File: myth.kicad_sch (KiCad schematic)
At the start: 151 parts, among them J1 Conn_01x08_Male, J2 Conn_01x08_Male, J4 Conn_01x08_Male, J5 Conn_01x08_Male, J6 Conn_01x08_Male, U1 74AHC02, U10 74HC595, U100 74AHC08, U101 74LS32, U102 74LS08, U103 74HC00, U104 74LS08, U105 74AHC02, U106 74LS08, U107 74LS08, U108 74LS08, U109 74LS573, U11 74HC165, U110 74LS573, U111 74HC157, U112 74HC157, U113 74HC157, U114 74AHC08, U115 4002, U116 4072, U117 74LS573, U118 74LS32, U119 74LS573, U12 74AHC08, U120 74LS573, U121 74AHC273, U122 74HC157, U123 74LS32, U124 74AHC04, U125 74LS573, U126 74LS573, U127 74AHC08, U128 74LS27, U129 74HC00, U13 74HC238, U130 74AHC08, U131 74LS573, U132 74HC74, U133 4072, U134 4072, U135 4078, U136 74AHC244, U137 74LS32, U138 74LS32, U139 74AHC273, U14 74HC238, U140 74LS32, U141 74LS32, U142 74AHC04, U15 74HC238, U16 4002, U17 74AHC273, U18 74LS32, U19 CD4532BE, U2 74AHC04, U20 74AHC138, U21 74AHC04, U22 74AHC138, U23 74HC238, U24 74HC238, U25 74LS32, U26 74AHC374, U27 74AHC244, U28 74HC238, U29 74HC238, U3 74HC74, U30 4075, U31 74AHC04, U32 74HC00, U33 74HC163, U34 74AHC138, U35 74AHC138, U36 74HC238, U37 74AHC138, U38 74LS32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

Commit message: Clarify xR instruction in spec
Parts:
- removed U18: 74LS32, Package_DIP:DIP-14_W7.62mm_Socket_LongPads, symbol 74xx:74LS32
- added U144: 74LS32, Package_DIP:DIP-14_W7.62mm_Socket_LongPads, symbol 74xx:74LS32
- added unit 1 of U30
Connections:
- net ~{CODE} is gone; now on net CODE: U98.1 (1OE), U98.19 (2OE)
- net COR: now also U30.2
- net RET: now also U30.8
- net SUBR: now also U30.1
- net xR: now also U144.13; no longer U57.11 (Cp)
- net at U12.11, U92.11 (Cp): now also U144.12
- net at U32.4: now also U30.9
- new net: U144.11, U57.11 (Cp)
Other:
- note added: "(Code Page Index)"
- note added: "(Resident Page Index)"
- note added: "0 DUP ("Copy of A") 1 SWAP ("Copy of X") 2 NOTA ("One's Complement of A") 3 NOTX ("One's Complement of X") 4 SLA ("Shift left A") 5 SLX ("Shift left X") 6 SRA ("Shift right A") 7 SRX ("Shift right X")"
- note added: "8 AND ("A boolean-and X") 9 IOR ("A inclusive-or X") 10 EOR ("A exclusive-or X") 11 ADD ("Add X to A) 12 CAR ("Carry bit of: A plus X") 13 ALX ("A less than X") 14 AEX ("A equal to X") 15 AGX ("A greater than X")"
- note added: "~{EXIT} (Can exit the current code page): PH3: Register target page-index CLOSE: Load into C"
- note removed: "(CODE Page-Index)"
- note removed: "(RESIDENT Page-Index)"
- note removed: "0 COA ("Copy of A - DUP") 1 COX ("Copy of X - SWAP") 2 OCA ("One's Complement of A") 3 OCX ("One's Complement of X") 4 ASL ("A shifted left") 5 XSL ("X shifted left") 6 ASR ("A shifted right") 7 XSR ("X shifted right")"
- note removed: "8 AND ("A boolean-and X") 9 IOR ("A inclusive-or X") 10 EOR ("A exclusive-or X") 11 SUM ("Sum of: X + A) 12 CAR ("Carry bit of: A plus X") 13 ALX ("A less than X") 14 AEX ("A equal to X") 15 AGX ("A greater than X")"
- note removed: "Code page index active when fetching instructions (IPH) or data literals (LFETCH/Fx)"
- note removed: "~{EXIT} (Exit the current code page): PH3: Register target page-index CLOSE: Load into C"
- moved on the sheet: U98

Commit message: Rename INC/DEC INCA/DECA for clarity
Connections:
- net DEC renamed DECA
- net INC renamed INCA
- net ~{DEC} renamed ~{DECA}
- net ~{INC} renamed ~{INCA}
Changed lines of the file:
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@@
 		)
 	)
-	(label "~{INC}"
+	(label "~{INCA}"
 		(at 906.78 86.36 180)
 		(effects
@@
 		)
 	)
-	(label "~{DEC}"
+	(label "~{DECA}"
 		(at 906.78 88.9 180)
 		(effects
@@
 		)
 	)
-	(label "DEC"
+	(label "DECA"
 		(at 303.53 262.89 0)
 		(effects
@@
 		)
 	)
-	(label "INC"
+	(label "INCA"
 		(at 303.53 265.43 0)
 		(effects

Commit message: Change CAR instruction to OVF combo
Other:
- note added: "8 AND ("A boolean-and X") 9 IOR ("A inclusive-or X") 10 EOR ("A exclusive-or X") 11 ADD ("Add X to A) 12 OVF ("Carry/Overflow of: A plus X") 13 ALX ("A less than X") 14 AEX ("A equal to X") 15 AGX ("A greater than X")"
- note added: "A := A & X A := A | X A := A ^ X A := A + X, bits 0-7 A := Zero + LSB=CARRY + MSB=OVERFLOW bit of: A+X A := (A<X)? 0xFF:0 A := (A==X)? 0xFF:0 A := (A>X)? 0xFF:0"
- note removed: "8 AND ("A boolean-and X") 9 IOR ("A inclusive-or X") 10 EOR ("A exclusive-or X") 11 ADD ("Add X to A) 12 CAR ("Carry bit of: A plus X") 13 ALX ("A less than X") 14 AEX ("A equal to X") 15 AGX ("A greater than X")"
- note removed: "A := A & X A := A | X A := A ^ X A := A + X, bits 0-7 A := 9th bit of: A+X, 0 or 1 A := (A<X)? 0xFF:0 A := (A==X)? 0xFF:0 A := (A>X)? 0xFF:0"
- moved on the sheet: J1, J2, J4, J5, J6, U104B, U106B, U106D, U107B, U109, U110, U111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

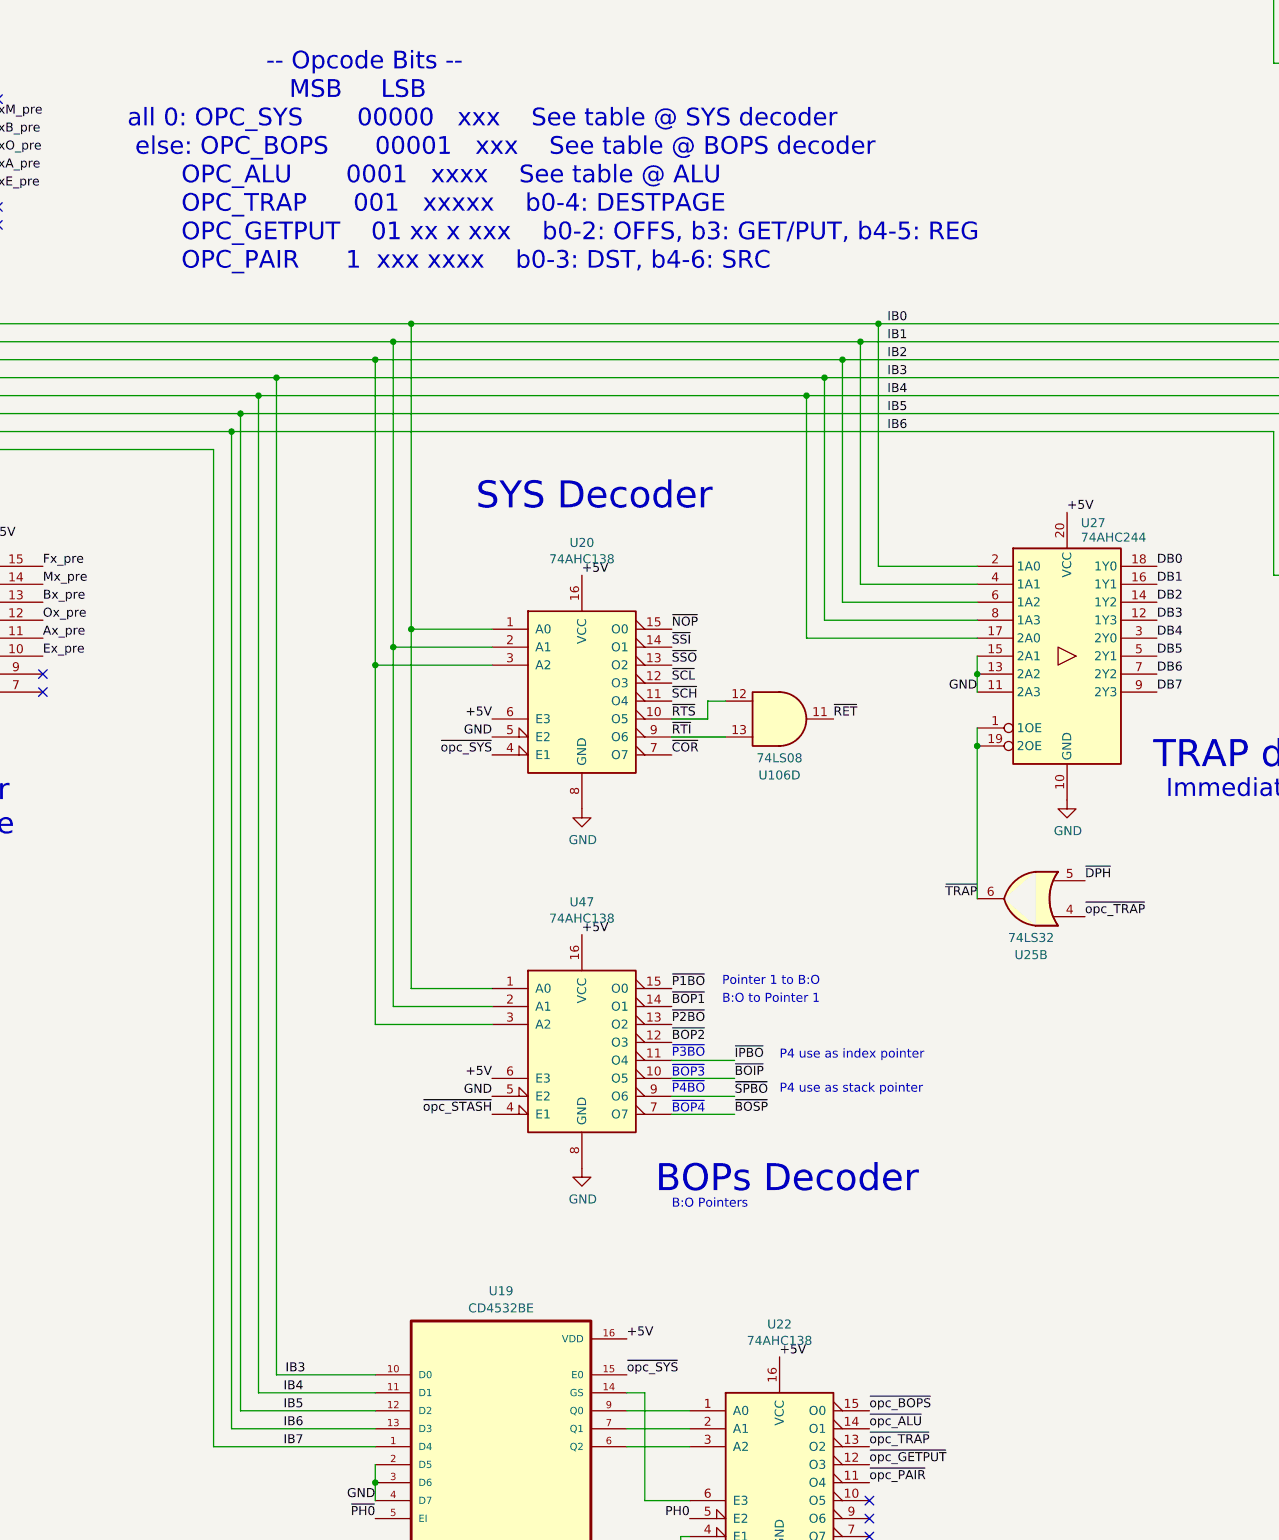
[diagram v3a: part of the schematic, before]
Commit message: Rename BOPS format group
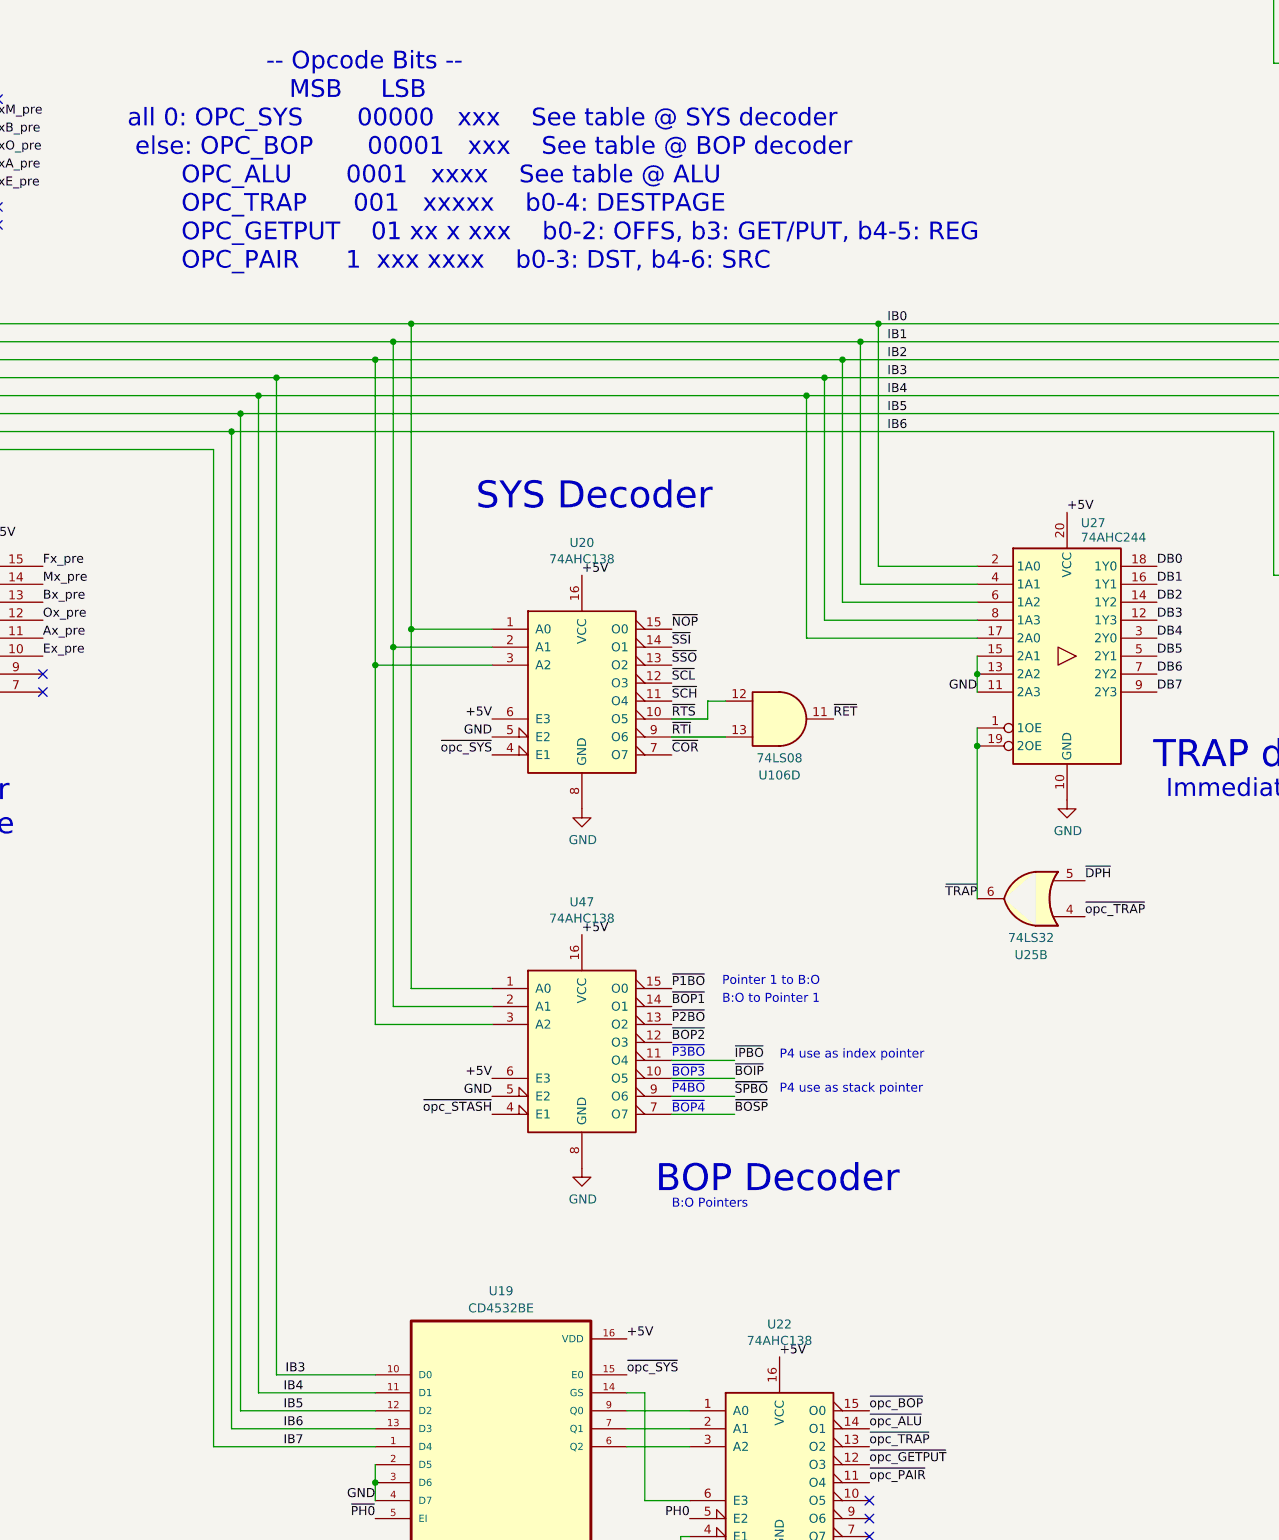
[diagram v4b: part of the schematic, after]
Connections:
- net ~{opc_BOPS} renamed ~{opc_BOP}
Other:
- note added: "-- Opcode Bits -- MSB LSB all 0: OPC_SYS 00000 xxx See table @ SYS decoder else: OPC_BOP 00001 xxx See table @ BOP decoder OPC_ALU 0001 xxxx See table @ ALU OPC_TRAP 001 xxxxx b0-4: DESTPAGE OPC_GETPUT 01 xx x xxx b0-2: OFFS, b3: GET/PUT, b4-5: REG OPC_PAIR 1 xxx xxxx b0-3: DST, b4-6: SRC"
- note added: "BOP Decoder"
- note removed: "-- Opcode Bits -- MSB LSB all 0: OPC_SYS 00000 xxx See table @ SYS decoder else: OPC_BOPS 00001 xxx See table @ BOPS decoder OPC_ALU 0001 xxxx See table @ ALU OPC_TRAP 001 xxxxx b0-4: DESTPAGE OPC_GETPUT 01 xx x xxx b0-2: OFFS, b3: GET/PUT, b4-5: REG OPC_PAIR 1 xxx xxxx b0-3: DST, b4-6: SRC"
- note removed: "BOPs Decoder"
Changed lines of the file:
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@@
 		)
 	)
-	(text "BOPs Decoder"
+	(text "BOP Decoder"
 		(exclude_from_sim no)
 		(at 288.544 452.12 0)
@@
 		)
 	)
-	(text "                  -- Opcode Bits --\n                     MSB     LSB\nall 0: OPC_SYS       00000   xxx    See table @ SYS decoder\n else: OPC_BOPS      00001   xxx    See table @ BOPS decoder\n       OPC_ALU       0001   xxxx    See table @ ALU\n       OPC_TRAP      001   xxxxx    b0-4: DESTPAGE\n       OPC_GETPUT    01 xx x xxx    b0-2: OFFS, b3: GET/PUT, b4-5: REG\n       OPC_PAIR      1  xxx xxxx    b0-3: DST, b4-6: SRC\n"
+	(text "                  -- Opcode Bits --\n                     MSB     LSB\nall 0: OPC_SYS       00000   xxx    See table @ SYS decoder\n else: OPC_BOP       00001   xxx    See table @ BOP decoder\n       OPC_ALU       0001   xxxx    See table @ ALU\n       OPC_TRAP      001   xxxxx    b0-4: DESTPAGE\n       OPC_GETPUT    01 xx x xxx    b0-2: OFFS, b3: GET/PUT, b4-5: REG\n       OPC_PAIR      1  xxx xxxx    b0-3: DST, b4-6: SRC\n"
 		(exclude_from_sim no)
 		(at 213.868 321.564 0)
@@
 		)
 	)
-	(label "~{opc_BOPS}"
+	(label "~{opc_BOP}"
 		(at 318.77 482.6 0)
 		(effects

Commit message: Fix comments in schematics file
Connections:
- net P3BO is gone; now on net LOCAL: U133.4
- net LOCAL: no longer U138.13
- new net IPBO: U138.13
- no-connect marks 44 -> 43
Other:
- note added: "A := A & X A := A | X A := A ^ X A := A + X, bits 0-7 A := Zero + LSB=CARRY + MSB=OVERFLOW bit of: A+X A := (A<X)? FFh:0 A := (A==X)? FFh:0 A := (A>X)? FFh:0"
- note added: "B: - Saves page index of current instruction byte during call/trap/cor - Outputs return page index during RET - Is the (only) implied page index for memory read-write, with the corresponding byte offset stored in O (Offset) - Together with O forms a 16-bit address pointers subject to the xU instruction The B:O pointer can be loaded from/saved into the BO-Pointers P1-4"
- note added: "F7h = 11110111b Corresponds to L0 in local page"
- note added: "O: - Saves offset of current instruction byte during call/trap/cor - Outputs return offset during RET - Is the (only) implied address offset for memory read-write, with the corresponding page index stored in B (Base) - Together with B forms 16-bit address pointers subject to the xU instruction. The B:O pointer can be loaded from/saved into the BO-Pointers P1-4"
- note added: "Put F7h on the bus O will latch"
- note added: "The L register is decremented during CALL/TRAP/ENTER and incremented during RET/LEAVE This operations provide single-page local stack frames for nested subroutines. Each local page has "GETPUT" variables called L1-L8 at byte offsets F8h-FFh. The LOCAL instruction sets B:O to L:F7h (L0)"
- note removed: "0xF7 = 0b11110111 Corresponds to L0 in local page"
- note removed: "A := A & X A := A | X A := A ^ X A := A + X, bits 0-7 A := Zero + LSB=CARRY + MSB=OVERFLOW bit of: A+X A := (A<X)? 0xFF:0 A := (A==X)? 0xFF:0 A := (A>X)? 0xFF:0"
- note removed: "B: - Saves page index of current instruction byte during call/trap/go - Outputs return page index during RET - Is the implied page index for memory read-write, with the corresponding byte offset stored in O (Offset) - Together with O forms a 16-bit address pointers subject to the xU instruction The B:O pointer can be loaded from/saved into the BO-Pointers P1-4"
- note removed: "O: - Saves offset of current instruction byte during call/trap/go - Outputs return offset during RET - Is the (only!) implied address offset for memory read-write, with the corresponding page index stored in B (Base) - Together with B forms 16-bit address pointers subject to the xU instruction. The B:O pointer can be loaded from/saved into the BO-Pointers P1-4"
- note removed: "Put 0xF7 on the bus O will latch"
- note removed: "The L register is decremented during CALL/TRAP/ENTER and incremented during RET/LEAVE This operations provide single-page local stack frames for nested subroutines. Each local page has "GETPUT" variables called L1-L8 at byte offsets 0xF8-0xFF."
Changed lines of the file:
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@@
 	(title_block
 		(title "Sonne-8 Micro-Controller")
-		(date "2025-06-05")
+		(date "2025-06-07")
 		(rev "Myth")
 		(company "Contact: mim@ok-schalter.de")
@@
 		)
 	)
-	(text "Put 0xF7 on the bus\nO will latch"
+	(text "Put F7h on the bus\nO will latch"
 		(exclude_from_sim no)
 		(at 563.88 615.188 0)
@@
 		)
 	)
-	(text "O:\n- Saves offset of current instruction byte during call/trap/go\n- Outputs return offset during RET\n- Is the (only!) implied address offset for memory read-write, with the corresponding page index stored in B (Base)\n- Together with B forms 16-bit address pointers subject to the xU instruction.\n  The B:O pointer can be loaded from/saved into the BO-Pointers P1-4"
+	(text "O:\n- Saves offset of current instruction byte during call/trap/cor\n- Outputs return offset during RET\n- Is the (only) implied address offset for memory read-write, with the corresponding page index stored in B (Base)\n- Together with B forms 16-bit address pointers subject to the xU instruction.\n  The B:O pointer can be loaded from/saved into the BO-Pointers P1-4"
 		(exclude_from_sim no)
 		(at 755.396 389.89 0)
@@
 		)
 	)
-	(text "A := A & X\nA := A | X\nA := A ^ X\nA := A + X, bits 0-7\nA := Zero + LSB=CARRY + MSB=OVERFLOW bit of: A+X\nA := (A<X)? 0xFF:0\nA := (A==X)? 0xFF:0\nA := (A>X)? 0xFF:0"
+	(text "A := A & X\nA := A | X\nA := A ^ X\nA := A + X, bits 0-7\nA := Zero + LSB=CARRY + MSB=OVERFLOW bit of: A+X\nA := (A<X)? FFh:0\nA := (A==X)? FFh:0\nA := (A>X)? FFh:0"
 		(exclude_from_sim no)
 		(at 799.338 151.638 0)
@@
 		)
 	)
-	(text "0xF7 = 0b11110111\nCorresponds to L0\nin local page"
+	(text "F7h = 11110111b\nCorresponds to L0\nin local page"
 		(exclude_from_sim no)
 		(at 513.334 593.598 0)
@@
 		)
 	)
-	(text "The L register is decremented during CALL/TRAP/ENTER\nand incremented during RET/LEAVE\n\nThis operations provide single-page local\nstack frames for nested subroutines.\n\nEach local page has \"GETPUT\" variables called\nL1-L8 at byte offsets 0xF8-0xFF.\n"
+	(text "The L register is decremented during CALL/TRAP/ENTER\nand incremented during RET/LEAVE\n\nThis operations provide single-page local\nstack frames for nested subroutines.\n\nEach local page has \"GETPUT\" variables called\nL1-L8 at byte offsets F8h-FFh.\n\nThe LOCAL instruction sets B:O to L:F7h (L0)"
 		(exclude_from_sim no)
-		(at 471.678 686.308 0)
+		(at 468.63 688.086 0)
 		(effects
 			(font
@@
 		)
 	)
-	(text "B:\n- Saves page index of current instruction byte during call/trap/go\n- Outputs return page index during RET\n- Is the implied page index for memory read-write, with the corresponding byte offset stored in O (Offset)\n- Together with O forms a 16-bit address pointers subject to the xU instruction\n  The B:O pointer can be loaded from/saved into the BO-Pointers P1-4"
+	(text "B:\n- Saves page index of current instruction byte during call/trap/cor\n- Outputs return page index during RET\n- Is the (only) implied page index for memory read-write, with the corresponding byte offset stored in O (Offset)\n- Together with O forms a 16-bit address pointers subject to the xU instruction\n  The B:O pointer can be loaded from/saved into the BO-Pointers P1-4"
 		(exclude_from_sim no)
 		(at 743.204 611.378 0)
@@
 	)
 	(no_connect
-		(at -88.9 438.15)
-	)
-	(no_connect
 		(at 196.85 245.11)
 	)
@@
 	)
 	(label "LOCAL"
-		(at 1083.31 596.9 180)
+		(at 1102.36 591.82 180)
 		(effects
 			(font
@@
 		)
 	)
-	(label "P3BO"
-		(at 1102.36 591.82 180)
+	(label "IPBO"
+		(at 1083.31 596.9 180)
 		(effects
 			(font
